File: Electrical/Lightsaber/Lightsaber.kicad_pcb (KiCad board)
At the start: 4 copper layers, 35 x 90 mm, 102 parts, among them J1 USB4105-GF-A, J2 locked, J3 54, J4 S2B-XH-A-1, J5 S2B-XH-A-1, J6 S2B-XH-A-1, J7 S3B-XH-A-1, J8 S3B-XH-A-1, Q1 BC817, Q2 BC817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

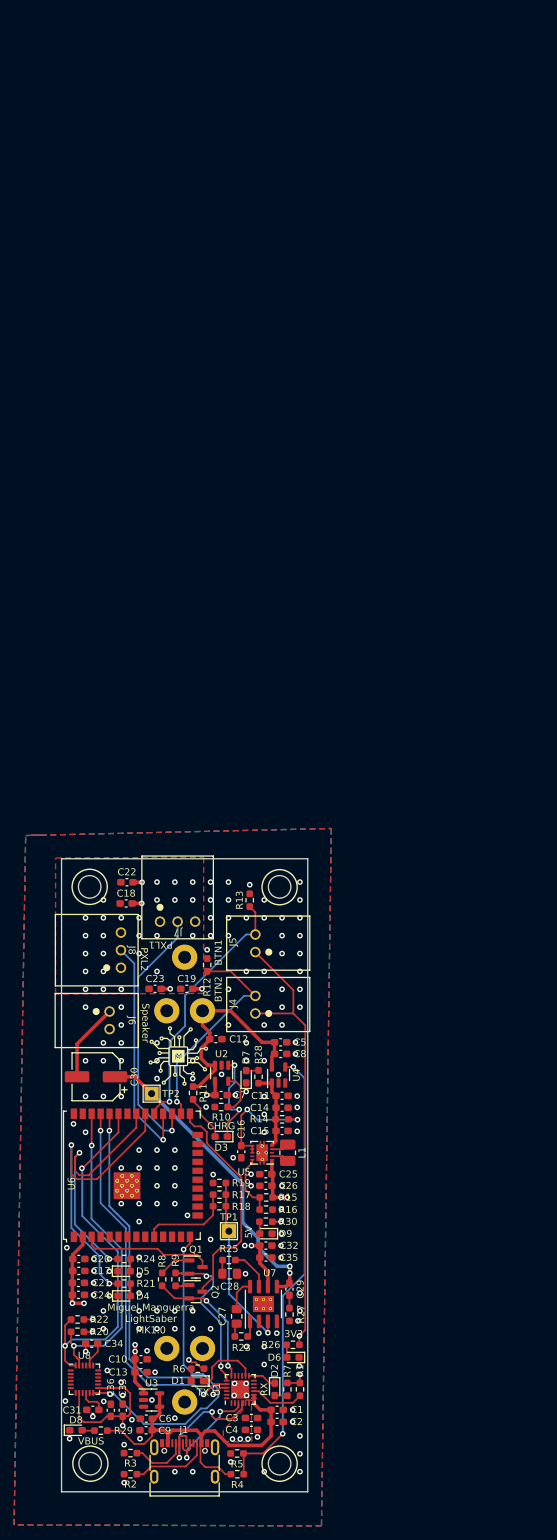
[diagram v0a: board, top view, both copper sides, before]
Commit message: Switched over to jst ph connectors
wrote test code as well
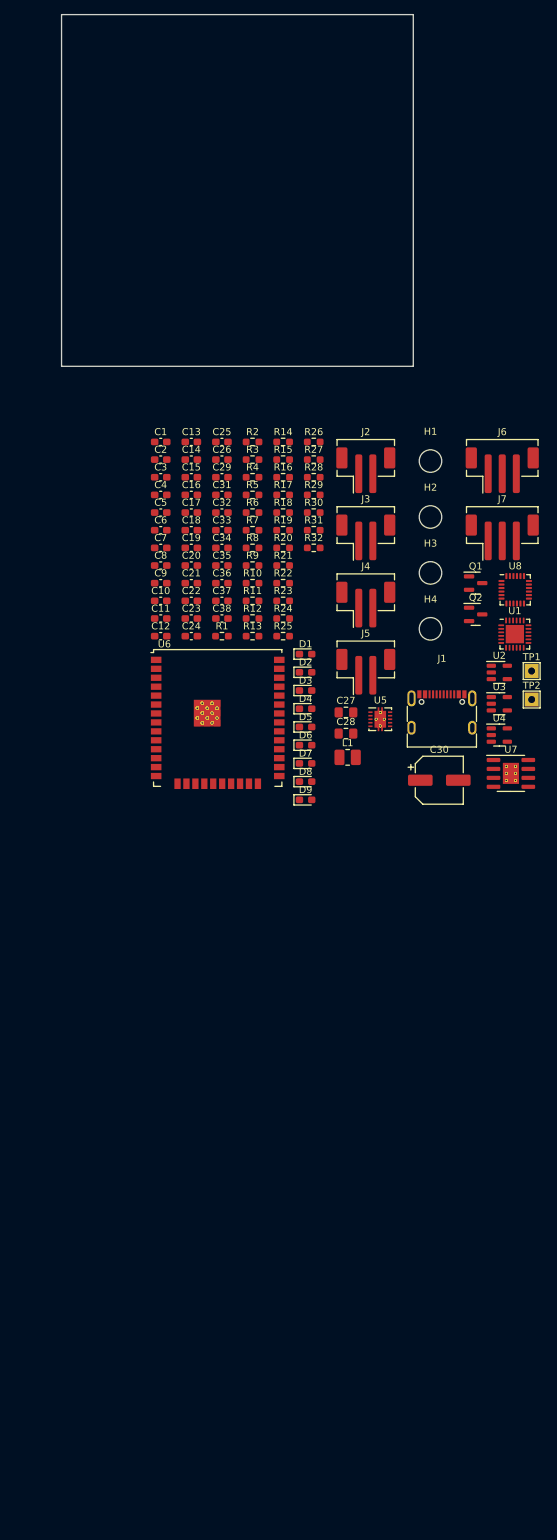
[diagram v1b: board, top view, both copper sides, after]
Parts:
- removed BT1: 18650 battery, Miguel:18650
- removed G***: LOGO, Miguel:Miguel Logo 10mm
- removed J8: S3B-XH-A-1, Miguel:S3B-XH-A-1
- added C37: 100n, Capacitor_SMD:C_0603_1608Metric_Pad1.08x0.95mm_HandSolder, F.Cu at (22.8, 83.3)
- added C38: 100n, Capacitor_SMD:C_0603_1608Metric_Pad1.08x0.95mm_HandSolder, F.Cu at (22.8, 85.8)
- added R31: 10kR, Resistor_SMD:R_0603_1608Metric_Pad0.98x0.95mm_HandSolder, F.Cu at (35.9, 73.3)
- added R32: 10kR, Resistor_SMD:R_0603_1608Metric_Pad0.98x0.95mm_HandSolder, F.Cu at (35.9, 75.8)
- J2: value locked -> B2B-PH-SM4-TB; footprint Miguel:54 -> Connector_JST:JST_PH_B2B-PH-SM4-TB_1x02-1MP_P2.00mm_Vertical; moved to F.Cu
- J3: value 54 -> B2B-PH-SM4-TB; footprint Miguel:54 -> Connector_JST:JST_PH_B2B-PH-SM4-TB_1x02-1MP_P2.00mm_Vertical; moved to F.Cu
- J4, J5: value S2B-XH-A-1 -> B2B-PH-SM4-TB; footprint Miguel:S2B-XH-A-1 -> Connector_JST:JST_PH_B2B-PH-SM4-TB_1x02-1MP_P2.00mm_Vertical
- J6: value S2B-XH-A-1 -> B3B-PH-SM4-TB; footprint Miguel:S2B-XH-A-1 -> Connector_JST:JST_PH_B3B-PH-SM4-TB_1x03-1MP_P2.00mm_Vertical
- J7: value S3B-XH-A-1 -> B3B-PH-SM4-TB; footprint Miguel:S3B-XH-A-1 -> Connector_JST:JST_PH_B3B-PH-SM4-TB_1x03-1MP_P2.00mm_Vertical
- moved R2 147.8 mm to (27.1, 60.8), turned to 0 degrees
- moved R3 142.3 mm to (27.1, 63.3), turned to 0 degrees
- moved R4 141.7 mm to (27.1, 65.8)
- moved C1 138.6 mm to (14.1, 60.8)
- moved C2 137.8 mm to (14.1, 63.3)
- moved R29 136.4 mm to (35.9, 68.3), turned to 0 degrees
- moved R5 136.3 mm to (27.1, 68.3), turned to 0 degrees
- moved H3 135.6 mm to (52.5, 79.4)
- moved C3 134.4 mm to (14.1, 65.8)
- moved C4 133.5 mm to (14.1, 68.3)
- moved C13 132.4 mm to (18.4, 60.8)
- moved C31 131.4 mm to (22.8, 68.3), turned to 0 degrees
- moved R26 128.4 mm to (35.9, 60.8), turned to 0 degrees
- moved U8 127.9 mm to (64.5, 81.8)
- moved C6 126.3 mm to (14.1, 73.3), turned to 0 degrees
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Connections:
- J3 pad 1: GND -> +3V3
- J4 pad 2: /BTN_1 -> /BTN_2
- J5 pad 1: +3V3 -> /SPKR_OUT
- J5 pad 2: /BTN_2 -> GND
- J6 pad 1: /SPKR_OUT -> +5V
- J6 pad 2: GND -> /DOUT_1
- J7 pad 2: /DOUT_1 -> /DOUT_2
- U1 pad 18: /DTR -> unconnected-(U1-~{CTS}-Pad18)
- U1 pad 23: unconnected-(U1-~{DTR}-Pad23) -> /DTR
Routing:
- net +3V3: track 106.3 -> 0.00 mm, vias 11 -> 0
- net /VBUS_EN: track 65.0 -> 0.00 mm, vias 2 -> 0
- net /RX: track 53.9 -> 0.00 mm, vias 2 -> 0
- net /TX: track 53.0 -> 0.00 mm, vias 2 -> 0
- net VBUS: track 52.2 -> 0.00 mm
- net /SDA: track 51.3 -> 0.00 mm, vias 2 -> 0
- net /INT: track 47.9 -> 0.00 mm, vias 2 -> 0
- net /SCL: track 45.9 -> 0.00 mm, vias 2 -> 0
- net Net-(C29-Pad1): track 45.0 -> 0.00 mm, vias 2 -> 0
- net /LED_1: track 43.3 -> 0.00 mm, vias 2 -> 0
- net /BTN_2: track 37.1 -> 0.00 mm, vias 1 -> 0
- net /DOUT_1: track 37.1 -> 0.00 mm, vias 1 -> 0
- net /LED_2: track 35.2 -> 0.00 mm, vias 2 -> 0
- net /DOUT_2: track 33.3 -> 0.00 mm, vias 1 -> 0
- net /BOOT: track 32.3 -> 0.00 mm
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- removed copper zone on F.Cu, net +3V3
- removed copper zone on In2.Cu, net +3V3
- removed copper zone on F.Cu, net +5V
- removed copper zone on In2.Cu, net +5V
- removed copper zone on In2.Cu, net +BATT
- removed copper zone on B.Cu, net GND
- removed copper zone on F.Cu, net GND
- removed copper zone on In1.Cu, net GND
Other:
- board size 35 x 90 mm -> 50 x 50 mm
- board text removed: "3V3"
- board text removed: "5V"
- board text removed: "BTN1"
- board text removed: "BTN2"
- board text removed: "CHRG"
- board text removed: "Miguel Manguerra LightSaber MK1.0"
- board text removed: "PXL1"
- board text removed: "PXL2"
- board text removed: "RX"
- board text removed: "Speaker"
- board text removed: "TX"
- board text removed: "VBUS"
